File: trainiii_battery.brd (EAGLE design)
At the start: 36 x 32 mm, 3 parts, among them J1 B3B-XH-A(LF)(SN), J2 B3B-XH-A(LF)(SN)

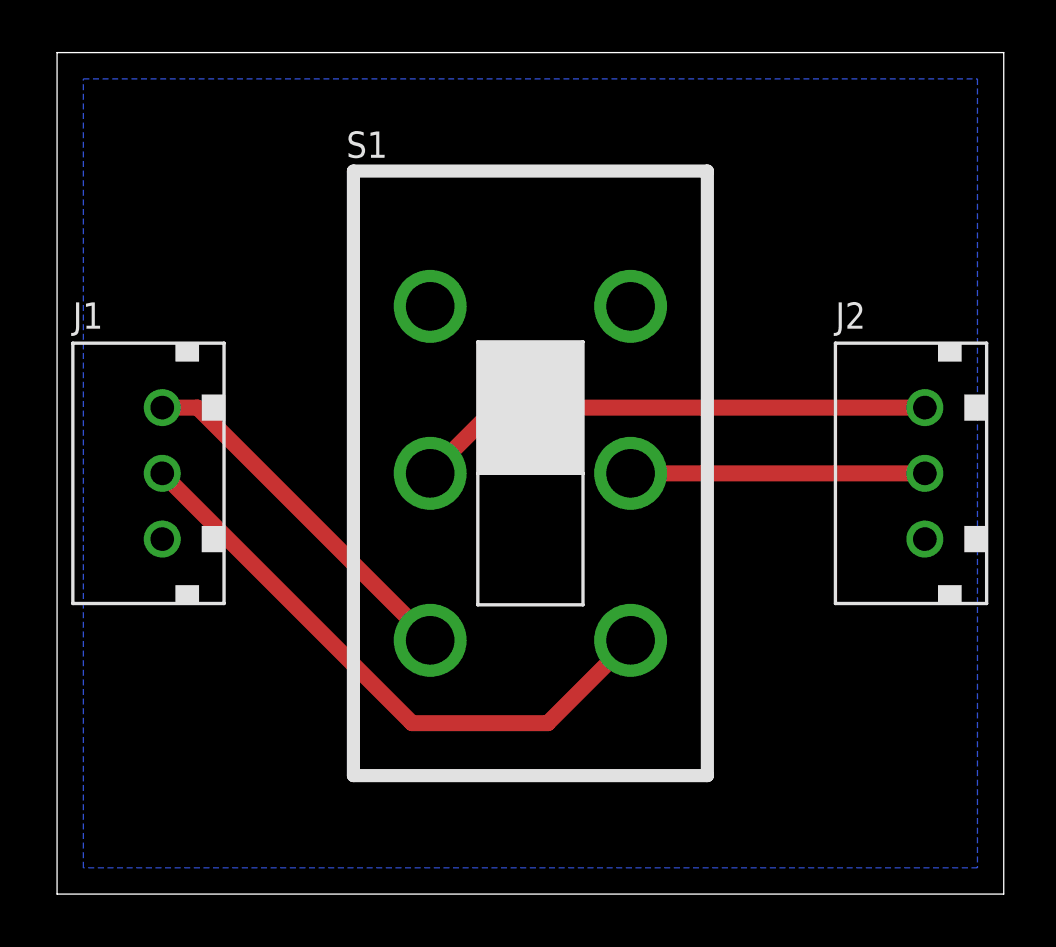
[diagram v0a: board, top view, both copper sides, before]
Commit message: Added status LED, cleaned up board layout
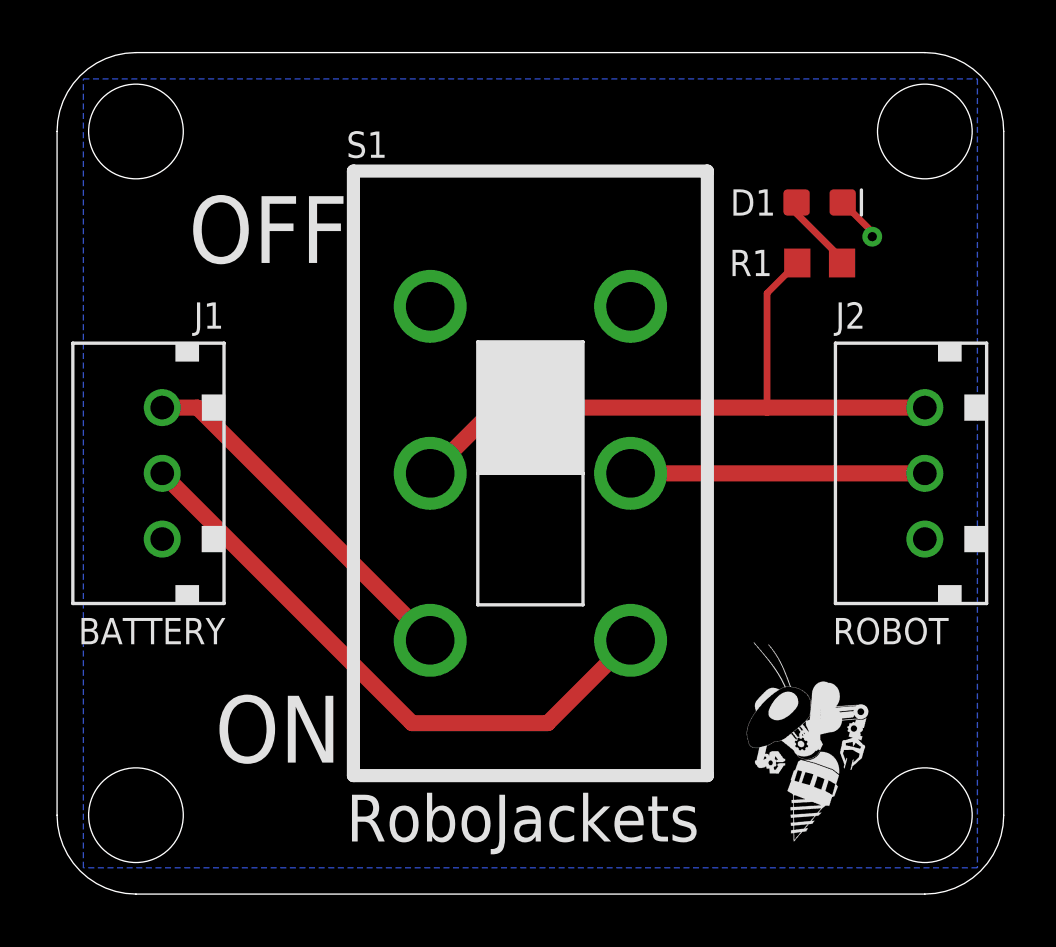
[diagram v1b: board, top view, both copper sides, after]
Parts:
- added D1: GRN, SparkFun-LED:LED-0603
- added R1: 330, rcl:R0603
- added U$2: (no value), RoboJackets-Aesthetics:ROBOBUZZ_0.4X
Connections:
- new net LED_IN: D1.A, R1.2
- net +VBAT_OUT: now also R1.1
- net GND: now also D1.C
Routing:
- net +VBAT_OUT: track 19.8 -> 25.8 mm
- net LED_IN: track 0.00 -> 3.02 mm
- net GND: track 0.00 -> 1.77 mm, vias 0 -> 1
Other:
- outline, holes or cut-outs redrawn
- board text added: "BATTERY"
- board text added: "OFF"
- board text added: "ON"
- board text added: "ROBOT"
- board text added: "RoboJackets"
- board text added: "Trainiii Battery Switch July 2019 v1.0"

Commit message: Final Order v1.0
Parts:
- R1: value 330 -> 510
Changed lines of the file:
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@@
 <drawing>
 <settings>
-<setting alwaysvectorfont="yes"/>
+<setting alwaysvectorfont="no"/>
 <setting verticaltext="up"/>
 </settings>
@@
 <text x="6.4" y="9.5" size="1" layer="21" font="vector" align="bottom-right">BATTERY</text>
 <text x="29.5" y="9.5" size="1" layer="21" font="vector">ROBOT</text>
-<text x="5" y="24" size="2.54" layer="21" font="vector" ratio="20">OFF</text>
+<text x="4.8" y="24" size="2.54" layer="21" font="vector" ratio="20">OFF</text>
 <text x="6" y="5" size="2.54" layer="21" font="vector" ratio="20">ON</text>
 <hole x="3" y="29" drill="3.6"/>
@@
 <attribute name="VALUE" x="14" y="28" size="1" layer="27" font="vector"/>
 </element>
-<element name="R1" library="rcl" library_urn="urn:adsk.eagle:library:334" package="R0603" package3d_urn="urn:adsk.eagle:package:23555/3" value="330" x="29" y="24" smashed="yes">
+<element name="R1" library="rcl" library_urn="urn:adsk.eagle:library:334" package="R0603" package3d_urn="urn:adsk.eagle:package:23555/3" value="510" x="29" y="24" smashed="yes">
 <attribute name="NAME" x="25.565" y="23.5" size="1" layer="25" font="vector"/>
 <attribute name="SPICEPREFIX" value="R" x="29" y="24" size="1.778" layer="27" display="off"/>
